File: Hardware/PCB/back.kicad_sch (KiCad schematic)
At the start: 52 parts, among them IC102 TL074, IC103 TL074, J901 AudioJack2_SwitchT, J902 AudioJack2, J903 AudioJack2, J904 AudioJack2, J905 AudioJack2_SwitchT, J906 AudioJack2, U7 NE5532, U901 L78L05_TO92, X101 RCA, X102 RCA

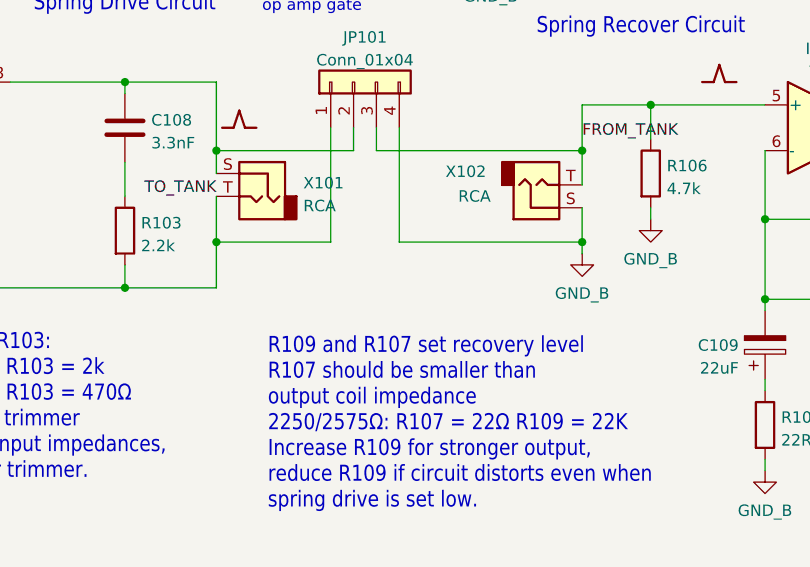
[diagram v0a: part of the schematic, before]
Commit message: Note on phono jacks, replace pin headers with Molex
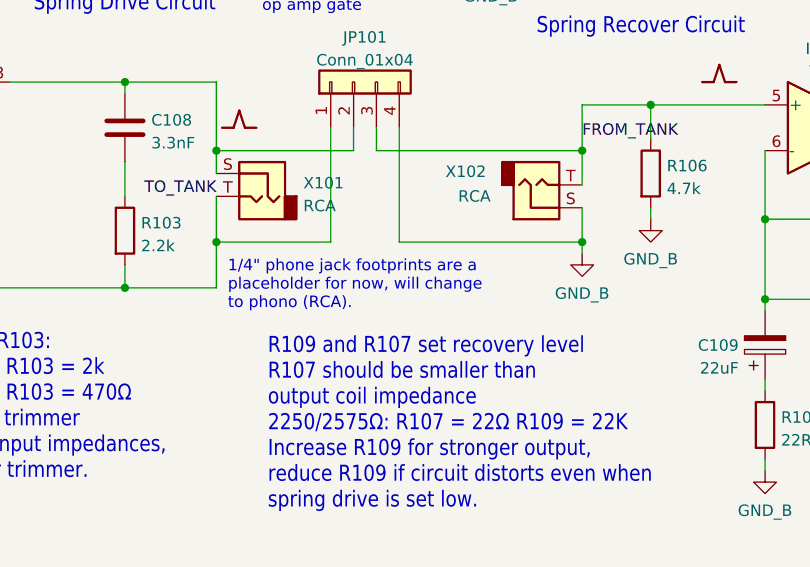
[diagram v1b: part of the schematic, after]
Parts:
- JP101: footprint Connector_PinHeader_2.54mm:PinHeader_1x04_P2.54mm_Vertical -> Connector_Molex:Molex_KK-254_AE-6410-04A_1x04_P2.54mm_Vertical
- JP102: footprint Connector_PinHeader_2.54mm:PinHeader_1x03_P2.54mm_Vertical -> ao_tht:Molex_KK-254_AE-6410-03A_1x03_P2.54mm_Vertical
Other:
- note added: "1/4" phone jack footprints are a placeholder for now, will change to phono (RCA)."
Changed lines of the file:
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@@
     (effects (font (size 1.778 1.5113)) (justify left bottom))
+  )
+  (text "1/4\" phone jack footprints are a\nplaceholder for now, will change \nto phono (RCA)."
+    (at 85.09 151.13 0)
+    (effects (font (size 1.27 1.27)) (justify left bottom))
   )
   (text "Ref numbers below 900 are\nsame as in original Music Thing\ndesign.\nRef no. 900+ are new (power \nreveral diodes and bypass caps \nadded, others are parts that\nhad no ref. no.)"
@@
     (property "Reference" "JP101" (id 0) (at 100.33 120.7602 90))
     (property "Value" "Conn_01x04" (id 1) (at 100.33 123.2971 90))
-    (property "Footprint" "Connector_PinHeader_2.54mm:PinHeader_1x04_P2.54mm_Vertical" (id 2) (at 99.06 125.73 0)
+    (property "Footprint" "Connector_Molex:Molex_KK-254_AE-6410-04A_1x04_P2.54mm_Vertical" (id 2) (at 99.06 125.73 0)
       (effects (font (size 1.27 1.27)) hide)
     )
@@
     (property "Reference" "JP102" (id 0) (at 157.48 108.0602 0))
     (property "Value" "Conn_01x03" (id 1) (at 157.48 110.5971 0))
-    (property "Footprint" "Connector_PinHeader_2.54mm:PinHeader_1x03_P2.54mm_Vertical" (id 2) (at 157.48 115.57 0)
-      (effects (font (size 1.27 1.27)) hide)
-    )
+    (property "Footprint" "ao_tht:Molex_KK-254_AE-6410-03A_1x03_P2.54mm_Vertical" (id 2) (at 157.48 115.57 0)
+      (effects (font (size 1.27 1.27)) hide)
+    )

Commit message: Layout redone
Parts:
- added H901, H902: MountingHole, ao_tht:MountingHole_3.2mm_M3, symbol ao_symbols:MountingHole
- C108, C110, C3, C4: footprint ao_tht:C_Disc_D3.0mm_W1.6mm_P2.50mm -> ao_tht:C_Rect_L7.2mm_W2.5mm_P5.00mm_FKS2_FKP2_MKS2_MKP2
- C5: footprint ao_tht:C_Disc_D3.0mm_W1.6mm_P2.50mm -> ao_tht:C_Disc_D5.0mm_W2.5mm_P5.00mm
- X101, X102: footprint ao_tht:Jack_6.35mm_PJ_629HAN_slots -> springreverb:RCJ-02
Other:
- note removed: "1/4" phone jack footprints are a placeholder for now, will change to phono (RCA)."
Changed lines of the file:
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@@
     (effects (font (size 1.778 1.5113)) (justify left bottom))
-  )
-  (text "1/4\" phone jack footprints are a\nplaceholder for now, will change \nto phono (RCA)."
-    (at 85.09 151.13 0)
-    (effects (font (size 1.27 1.27)) (justify left bottom))
   )
   (text "Ref numbers below 900 are\nsame as in original Music Thing\ndesign.\nRef no. 900+ are new (power \nreveral diodes and bypass caps \nadded, others are parts that\nhad no ref. no.)"
@@
     (property "Reference" "C4" (id 0) (at 222.25 36.0512 90))
     (property "Value" "33nF" (id 1) (at 222.25 38.5881 90))
-    (property "Footprint" "ao_tht:C_Disc_D3.0mm_W1.6mm_P2.50mm" (id 2) (at 226.06 40.9448 0)
+    (property "Footprint" "ao_tht:C_Rect_L7.2mm_W2.5mm_P5.00mm_FKS2_FKP2_MKS2_MKP2" (id 2) (at 226.06 40.9448 0)
       (effects (font (size 1.27 1.27)) hide)
     )
@@
     (property "Reference" "C110" (id 0) (at 156.21 144.0012 90))
     (property "Value" "2.2nF" (id 1) (at 156.21 146.5381 90))
-    (property "Footprint" "ao_tht:C_Disc_D3.0mm_W1.6mm_P2.50mm" (id 2) (at 160.02 148.8948 0)
+    (property "Footprint" "ao_tht:C_Rect_L7.2mm_W2.5mm_P5.00mm_FKS2_FKP2_MKS2_MKP2" (id 2) (at 160.02 148.8948 0)
       (effects (font (size 1.27 1.27)) hide)
     )
@@
       (effects (font (size 1.27 1.27)) (justify right))
     )
-    (property "Footprint" "ao_tht:Jack_6.35mm_PJ_629HAN_slots" (id 2) (at 88.9 138.43 0)
+    (property "Footprint" "springreverb:RCJ-02" (id 2) (at 88.9 138.43 0)
       (effects (font (size 1.27 1.27)) hide)
     )
@@
     (property "Reference" "C5" (id 0) (at 233.68 58.9112 90))
     (property "Value" "22pF" (id 1) (at 233.68 61.4481 90))
-    (property "Footprint" "ao_tht:C_Disc_D3.0mm_W1.6mm_P2.50mm" (id 2) (at 237.49 63.8048 0)
+    (property "Footprint" "ao_tht:C_Disc_D5.0mm_W2.5mm_P5.00mm" (id 2) (at 237.49 63.8048 0)
       (effects (font (size 1.27 1.27)) hide)
     )
@@
     (property "Reference" "C3" (id 0) (at 207.01 48.7512 90))
     (property "Value" "33nF" (id 1) (at 207.01 51.2881 90))
-    (property "Footprint" "ao_tht:C_Disc_D3.0mm_W1.6mm_P2.50mm" (id 2) (at 210.82 53.6448 0)
+    (property "Footprint" "ao_tht:C_Rect_L7.2mm_W2.5mm_P5.00mm_FKS2_FKP2_MKS2_MKP2" (id 2) (at 210.82 53.6448 0)
       (effects (font (size 1.27 1.27)) hide)
     )
@@
     )
   )
+  (symbol (lib_id "ao_symbols:MountingHole") (at 123.19 184.15 0) (unit 1)
+    (in_bom no) (on_board yes) (fields_autoplaced)
+    (property "Reference" "H901" (id 0) (at 125.73 183.3153 0)
+      (effects (font (size 1.27 1.27)) (justify left))
+    )
+    (property "Value" "MountingHole" (id 1) (at 125.73 185.8522 0)
+      (effects (font (size 1.27 1.27)) (justify left))
+    )
+    (property "Footprint" "ao_tht:MountingHole_3.2mm_M3" (id 2) (at 123.19 184.15 0)
+      (effects (font (size 1.27 1.27)) hide)
+    )
+    (property "Datasheet" "" (id 3) (at 123.19 184.15 0)
+      (effects (font (size 1.27 1.27)) hide)
+    )
+    (property "Config" "DNF" (id 4) (at 123.19 184.15 0)
+      (effects (font (size 1.27 1.27)) hide)
+    )
+  )
   (symbol (lib_id "ao_symbols:R") (at 236.22 54.61 90) (unit 1)
     (in_bom yes) (on_board yes) (fields_autoplaced)
@@
       (effects (font (size 1.27 1.27)) (justify left))
     )
-    (property "Footprint" "ao_tht:C_Disc_D3.0mm_W1.6mm_P2.50mm" (id 2) (at 74.6252 134.62 0)
+    (property "Footprint" "ao_tht:C_Rect_L7.2mm_W2.5mm_P5.00mm_FKS2_FKP2_MKS2_MKP2" (id 2) (at 74.6252 134.62 0)
       (effects (font (size 1.27 1.27)) hide)
     )
@@
       (effects (font (size 1.27 1.27)) (justify right))
     )
-    (property "Footprint" "ao_tht:Jack_6.35mm_PJ_629HAN_slots" (id 2) (at 119.38 137.16 0)
+    (property "Footprint" "springreverb:RCJ-02" (id 2) (at 119.38 137.16 0)
       (effects (font (size 1.27 1.27)) hide)
     )
@@
     (pin "1")
   )
+  (symbol (lib_id "ao_symbols:MountingHole") (at 142.24 184.15 0) (unit 1)
+    (in_bom no) (on_board yes) (fields_autoplaced)
+    (property "Reference" "H902" (id 0) (at 144.78 183.3153 0)
+      (effects (font (size 1.27 1.27)) (justify left))
+    )
+    (property "Value" "MountingHole" (id 1) (at 144.78 185.8522 0)
+      (effects (font (size 1.27 1.27)) (justify left))
+    )
+    (property "Footprint" "ao_tht:MountingHole_3.2mm_M3" (id 2) (at 142.24 184.15 0)
+      (effects (font (size 1.27 1.27)) hide)
+    )
+    (property "Datasheet" "" (id 3) (at 142.24 184.15 0)
+      (effects (font (size 1.27 1.27)) hide)
+    )
+    (property "Config" "DNF" (id 4) (at 142.24 184.15 0)
+      (effects (font (size 1.27 1.27)) hide)
+    )
+  )
   (symbol (lib_id "ao_symbols:Graphic") (at 128.27 190.5 0) (unit 1)

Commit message: phono jacks
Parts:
- V101: footprint OptoDevice:PerkinElmer_VTL5C -> ao_tht:Vactrol_VTL5C
- X101: footprint springreverb:RCJ-02 -> springreverb:RCJ-023 white
- X102: footprint springreverb:RCJ-02 -> springreverb:RCJ-022 red
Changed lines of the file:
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@@
     (property "Reference" "V101" (id 0) (at 76.2 52.1802 0))
     (property "Value" "32SR3 OR VTL5C3" (id 1) (at 76.2 54.7171 0))
-    (property "Footprint" "OptoDevice:PerkinElmer_VTL5C" (id 2) (at 76.2 59.69 0)
+    (property "Footprint" "ao_tht:Vactrol_VTL5C" (id 2) (at 76.2 59.69 0)
       (effects (font (size 1.27 1.27)) hide)
     )
@@
       (effects (font (size 1.27 1.27)) (justify right))
     )
-    (property "Footprint" "springreverb:RCJ-02" (id 2) (at 88.9 138.43 0)
+    (property "Footprint" "springreverb:RCJ-023 white" (id 2) (at 88.9 138.43 0)
       (effects (font (size 1.27 1.27)) hide)
     )
@@
       (effects (font (size 1.27 1.27)) (justify right))
     )
-    (property "Footprint" "springreverb:RCJ-02" (id 2) (at 119.38 137.16 0)
-      (effects (font (size 1.27 1.27)) hide)
-    )
+    (property "Footprint" "springreverb:RCJ-022 red" (id 2) (at 119.38 137.16 0)
+      (effects (font (size 1.27 1.27)) hide)
+    )
